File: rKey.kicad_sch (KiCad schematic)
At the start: 41 parts, among them IC1 BDX34C, J1 Conn_01x06, K1 RT42xxxx, Q1 BC337, Q2 BC337, Q3 BC337, Q4 BC337, Q5 BC327, Q8 BC337, U1 TL084BCN, U2 LM7810_TO220

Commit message: small fixes...
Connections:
- net GND: now also K1.22
- net at J1.3 (Pin_3), K1.11, R13.2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: now also K1.21
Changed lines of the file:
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@@
   (junction (at 180.975 107.95) (diameter 0) (color 0 0 0 0)
+  )
+  (junction (at 113.538 45.72) (diameter 0) (color 0 0 0 0)
   )
   (junction (at 169.545 73.66) (diameter 0) (color 0 0 0 0)
@@
     (stroke (width 0) (type default) (color 0 0 0 0))
   )
+  (wire (pts (xy 113.538 45.72) (xy 113.538 35.56))
+    (stroke (width 0) (type default) (color 0 0 0 0))
+  )
   (wire (pts (xy 89.535 92.71) (xy 89.535 95.25))
     (stroke (width 0) (type default) (color 0 0 0 0))
@@
     (stroke (width 0) (type default) (color 0 0 0 0))
   )
+  (wire (pts (xy 113.538 45.72) (xy 124.46 45.72))
+    (stroke (width 0) (type default) (color 0 0 0 0))
+  )
   (wire (pts (xy 224.282 56.642) (xy 224.155 90.805))
     (stroke (width 0) (type default) (color 0 0 0 0))
@@
     (stroke (width 0) (type default) (color 0 0 0 0))
   )
-  (wire (pts (xy 105.156 45.72) (xy 124.46 45.72))
+  (wire (pts (xy 105.156 45.72) (xy 113.538 45.72))
     (stroke (width 0) (type default) (color 0 0 0 0))
   )
@@
     (stroke (width 0) (type default) (color 0 0 0 0))
   )
+  (wire (pts (xy 85.852 48.26) (xy 85.852 38.1))
+    (stroke (width 0) (type default) (color 0 0 0 0))
+  )
   (wire (pts (xy 55.88 76.2) (xy 47.625 76.2))
     (stroke (width 0) (type default) (color 0 0 0 0))
@@
     (stroke (width 0) (type default) (color 0 0 0 0))
   )
+  (wire (pts (xy 113.538 35.56) (xy 105.156 35.56))
+    (stroke (width 0) (type default) (color 0 0 0 0))
+  )
   (wire (pts (xy 180.975 92.075) (xy 180.975 95.885))
     (stroke (width 0) (type default) (color 0 0 0 0))
@@
     (stroke (width 0) (type default) (color 0 0 0 0))
   )
+  (wire (pts (xy 85.852 38.1) (xy 89.916 38.1))
+    (stroke (width 0) (type default) (color 0 0 0 0))
+  )

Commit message: fixes
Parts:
- removed D1: DIODE, Diode_THT:D_DO-34_SOD68_P7.62mm_Horizontal, symbol pspice:DIODE
- added C2: 150uF, Capacitor_THT:CP_Radial_D7.5mm_P2.50mm, symbol Device:C_Polarized
- added Q6, Q9: BC327, Package_TO_SOT_THT:TO-92L_Inline_Wide, symbol Transistor_BJT:BC327
- added Q7: BC337, Package_TO_SOT_THT:TO-92L_Inline_Wide, symbol Transistor_BJT:BC337
- added R18: 50K, Resistor_THT:R_Axial_DIN0204_L3.6mm_D1.6mm_P5.08mm_Horizontal, symbol Device:R
- added R19, R20: 20K, Resistor_THT:R_Axial_DIN0204_L3.6mm_D1.6mm_P5.08mm_Horizontal, symbol Device:R
- added R21: 200K, Resistor_THT:R_Axial_DIN0204_L3.6mm_D1.6mm_P5.08mm_Horizontal, symbol Device:R
- added R22: 10K, Resistor_THT:R_Axial_DIN0204_L3.6mm_D1.6mm_P5.08mm_Horizontal, symbol Device:R
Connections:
- net GND: now also C2.2, Q9.1 (C)
- net at J1.3 (Pin_3), K1.11, K1.21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: now also R22.2
- net at R1.1, R14.1, RVa_max1.1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: now also Q6.3 (E), R18.1, R21.2
- net at J1.6 (Pin_6), K1.A2, R9.2: now also Q6.1 (C)
- new net: Q9.2 (B), R22.1
- new net: Q7.2 (B), R18.2
- new net: C2.1, Q7.3 (E), R20.1
- new net: Q9.3 (E), R20.2
- new net: Q6.2 (B), R19.1
- new net: Q7.1 (C), R19.2, R21.1
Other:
- moved on the sheet: K1

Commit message: fix
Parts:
- removed R6: 20, Resistor_THT:R_Axial_Power_L20.0mm_W6.4mm_P22.40mm, symbol Device:R
- R1: footprint Resistor_THT:R_Axial_DIN0207_L6.3mm_D2.5mm_P10.16mm_Horizontal -> Resistor_THT:R_Axial_Power_L20.0mm_W6.4mm_P22.40mm
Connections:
- net at IC1.3 (E), J1.5 (Pin_5), R11.2: now also U2.1 (VI)
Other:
- note removed: "(600mA max)"
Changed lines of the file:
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@@
-    (stroke (width 0) (type default) (color 0 0 0 0))
-  )
-  (wire (pts (xy 105.41 128.27) (xy 172.72 128.27))
     (stroke (width 0) (type default) (color 0 0 0 0))
   )
@@
     (stroke (width 0) (type default) (color 0 0 0 0))
   )
-  (wire (pts (xy 75.565 128.27) (xy 97.79 128.27))
+  (wire (pts (xy 75.565 128.27) (xy 172.72 128.27))
     (stroke (width 0) (type default) (color 0 0 0 0))
   )
@@
   (wire (pts (xy 219.075 51.562) (xy 248.92 51.562))
     (stroke (width 0) (type default) (color 0 0 0 0))
-  )
-  (text "(600mA max)" (at 95.25 132.715 0)
-    (effects (font (size 1.27 1.27)) (justify left bottom))
   )
   (text "1) RA\n2) RA\n3) RB\n4) RB\n5) VCC(out)\n6) VCC(in)" (at 26.035 88.9 0)
@@
       (effects (font (size 1.27 1.27)) (justify left))
     )
-    (property "Footprint" "Resistor_THT:R_Axial_DIN0207_L6.3mm_D2.5mm_P10.16mm_Horizontal" (id 2) (at 54.102 70.485 90)
+    (property "Footprint" "Resistor_THT:R_Axial_Power_L20.0mm_W6.4mm_P22.40mm" (id 2) (at 54.102 70.485 90)
       (effects (font (size 1.27 1.27)) hide)
     )
@@
     (pin "3")
   )
-  (symbol (lib_id "Device:R") (at 101.6 128.27 90) (unit 1)
-    (in_bom yes) (on_board yes)
-    (property "Reference" "R6" (id 0) (at 101.6 126.238 90)
-      (effects (font (size 1.27 1.27)) hide)
-    )
-    (property "Value" "20" (id 1) (at 101.6 128.27 90))
-    (property "Footprint" "Resistor_THT:R_Axial_Power_L20.0mm_W6.4mm_P22.40mm" (id 2) (at 101.6 130.048 90)
-      (effects (font (size 1.27 1.27)) hide)
-    )
-    (property "Datasheet" "~" (id 3) (at 101.6 128.27 0)
-      (effects (font (size 1.27 1.27)) hide)
-    )
-    (pin "1")
-    (pin "2")
-  )
   (symbol (lib_id "Device:R") (at 89.662 108.712 0) (unit 1)
     (in_bom yes) (on_board yes)
@@
     )
     (path "/72002845-30e6-48b4-aa12-d0584bfbc710"
-      (reference "R1") (unit 1) (value "100") (footprint "Resistor_THT:R_Axial_DIN0207_L6.3mm_D2.5mm_P10.16mm_Horizontal")
+      (reference "R1") (unit 1) (value "100") (footprint "Resistor_THT:R_Axial_Power_L20.0mm_W6.4mm_P22.40mm")
     )
     (path "/7eeaf7b2-ec17-42b5-b11d-32bf4db6bec1"
@@
       (reference "R5") (unit 1) (value "6K") (footprint "Resistor_THT:R_Axial_DIN0204_L3.6mm_D1.6mm_P5.08mm_Horizontal")
     )
-    (path "/cb03f869-1ffd-4659-9e77-af2508cdd04f"
-      (reference "R6") (unit 1) (value "20") (footprint "Resistor_THT:R_Axial_Power_L20.0mm_W6.4mm_P22.40mm")
-    )
     (path "/706e509c-5c98-4163-a906-7f1ab9d72bf9"

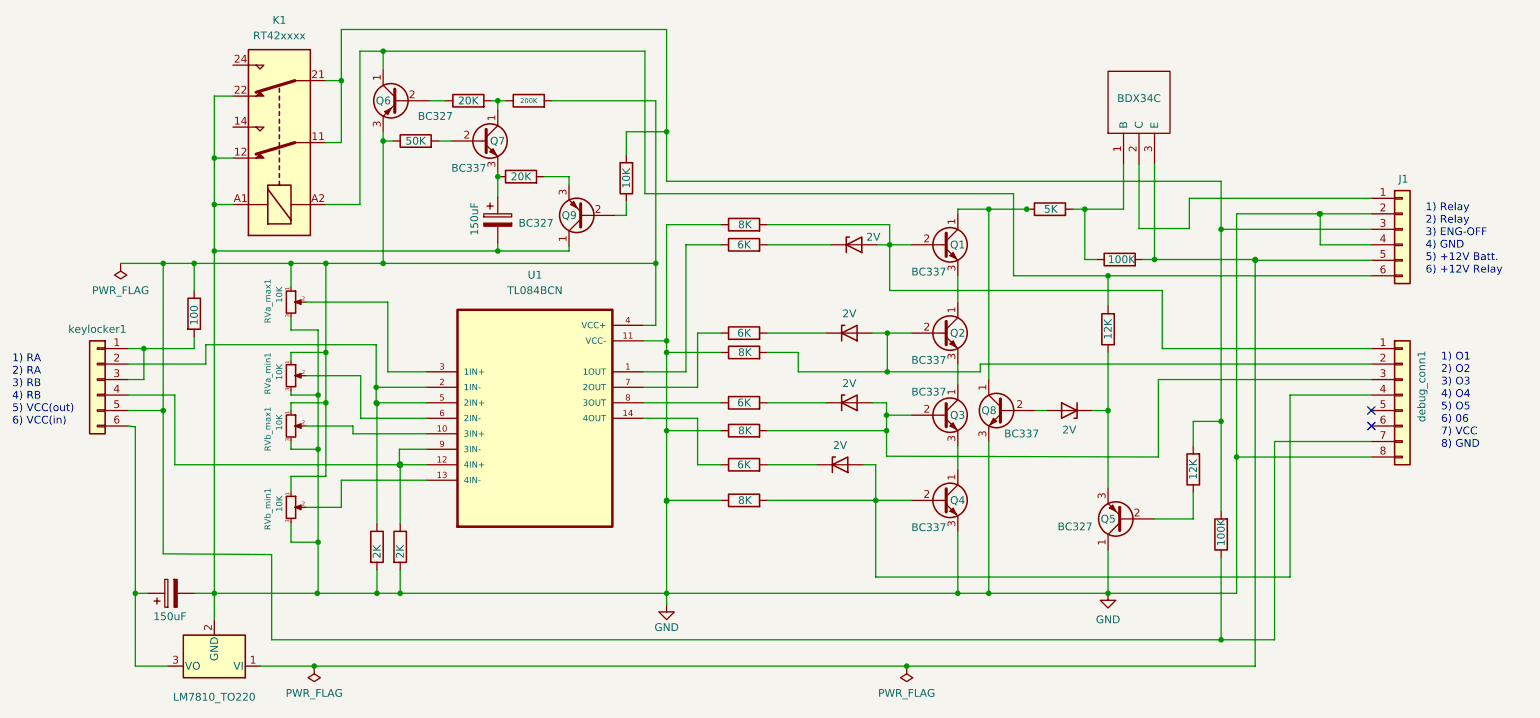
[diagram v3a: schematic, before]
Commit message: Enhancements and fixes
1) the generic rerlay has been replaced by HK19F
2) unuseful components have been removed
3) pull-down resistors resizing from 8K to more common 10K
4) the 12K resistor linked to the BC237 IC's emiotter, has been resized from 12K to 6K
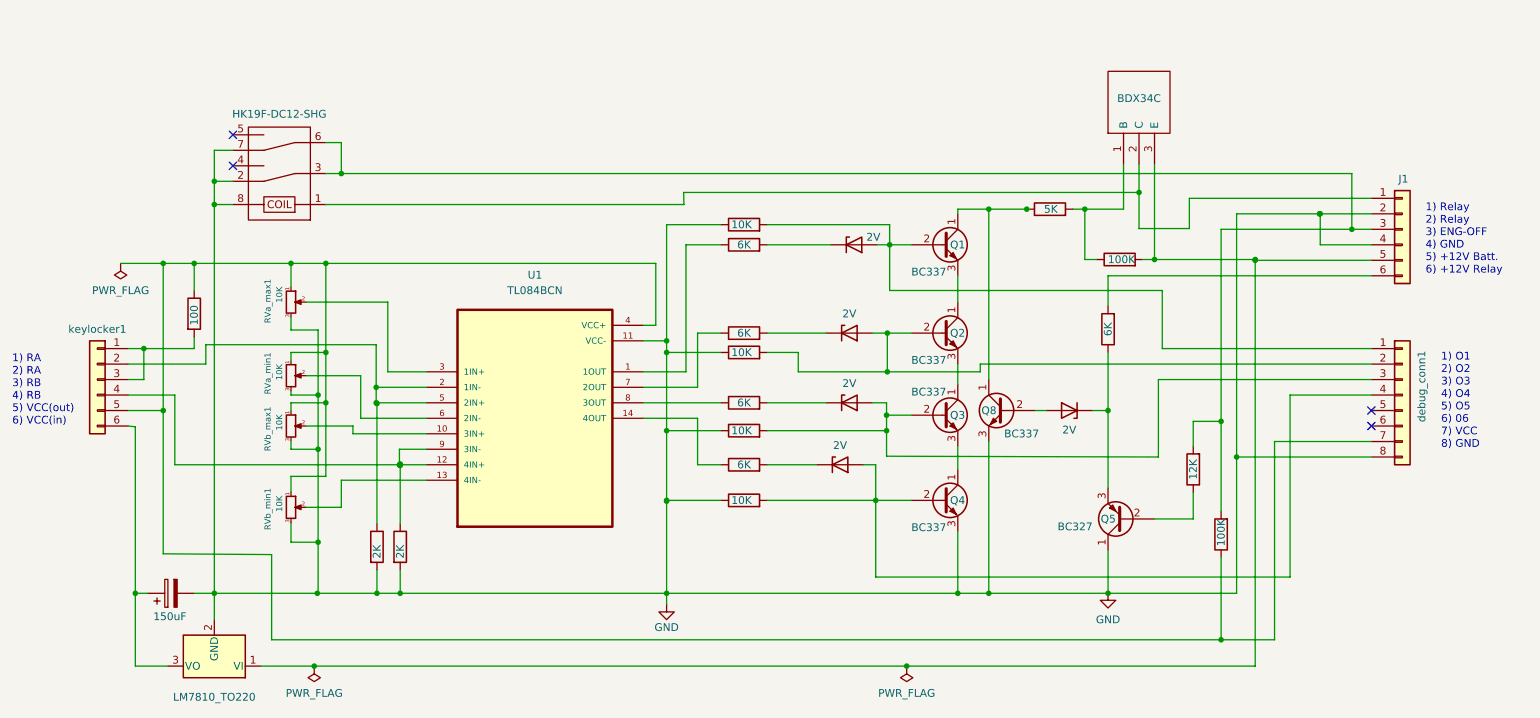
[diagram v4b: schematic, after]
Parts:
- removed C2: 150uF, Capacitor_THT:CP_Radial_D7.5mm_P2.50mm, symbol Device:C_Polarized
- removed K1: RT42xxxx, Relay_THT:Relay_DPDT_Schrack-RT2-FormC_RM5mm, symbol Relay:RT42xxxx
- removed Q6, Q9: BC327, Package_TO_SOT_THT:TO-92L_Inline_Wide, symbol Transistor_BJT:BC327
- removed Q7: BC337, Package_TO_SOT_THT:TO-92L_Inline_Wide, symbol Transistor_BJT:BC337
- removed R18: 50K, Resistor_THT:R_Axial_DIN0204_L3.6mm_D1.6mm_P5.08mm_Horizontal, symbol Device:R
- removed R19, R20: 20K, Resistor_THT:R_Axial_DIN0204_L3.6mm_D1.6mm_P5.08mm_Horizontal, symbol Device:R
- removed R21: 200K, Resistor_THT:R_Axial_DIN0204_L3.6mm_D1.6mm_P5.08mm_Horizontal, symbol Device:R
- removed R22: 10K, Resistor_THT:R_Axial_DIN0204_L3.6mm_D1.6mm_P5.08mm_Horizontal, symbol Device:R
- added U3: HK19F-DC12-SHG, HK19F:HK19F-DC12-SHG, symbol HK19F:HK19F-DC12-SHG
- R12, R15, R16, R17: value 8K -> 10K
- R9: value 12K -> 6K
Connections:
- net GND: now also U3.2, U3.7, U3.8
- net at J1.3 (Pin_3), R13.2, R14.2: now also U3.3, U3.6
- net at IC1.2 (C), J1.1 (Pin_1): now also U3.1
- no-connect marks 2 -> 4
